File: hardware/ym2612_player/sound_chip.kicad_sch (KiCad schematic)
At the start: 30 parts, among them U3 74HCT541, U4 74HCT541, U5 YM2612 (socket only, chip fit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, X1 7.670454 MHz, 5V (not fitted)

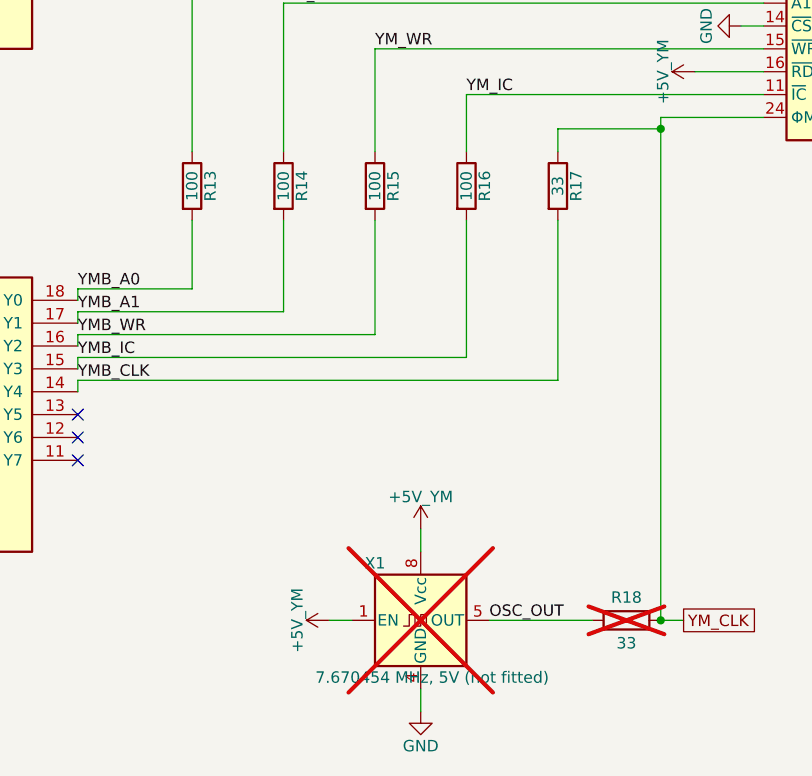
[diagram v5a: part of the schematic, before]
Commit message: Schematic: R13-R18 pin 1 back on the same net as on the board
The wired redraw drew R13-R17 upright and R18 turned, and swapped which net went to pin 1.
A resistor doesn't care, but KiCad's board-vs-schematic check flags it. Turn the symbols
instead, so every pin matches the board's pads again (checked pad by pad: 0 differences).

Co-Authored-By: Claude Opus 5.5 <noreply@anthropic.com>
Claude-Session: https://claude.ai/code/session_01TDTDVidYRoyJdUGgsyVTSw
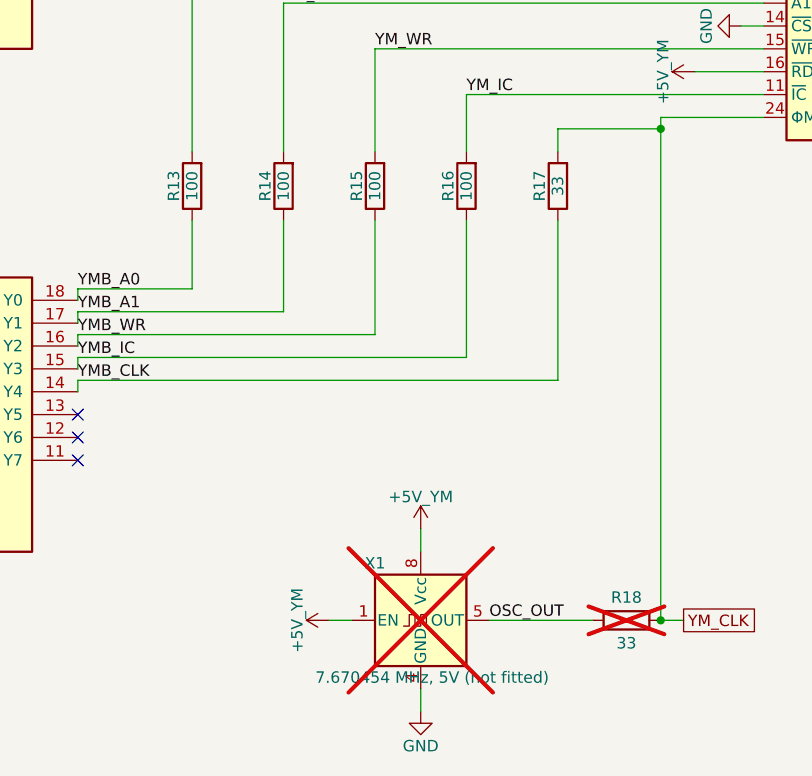
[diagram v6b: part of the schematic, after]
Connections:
- net OSC_OUT: now also R18.1; no longer R18.2
- net YMB_A0: now also R13.1; no longer R13.2
- net YMB_A1: now also R14.1; no longer R14.2
- net YMB_CLK: now also R17.1; no longer R17.2
- net YMB_IC: now also R16.1; no longer R16.2
- net YMB_WR: now also R15.1; no longer R15.2
- net YM_A0: now also R13.2; no longer R13.1
- net YM_A1: now also R14.2; no longer R14.1
- net YM_CLK: now also R17.2, R18.2; no longer R17.1, R18.1
- net YM_IC: now also R16.2; no longer R16.1
- net YM_WR: now also R15.2; no longer R15.1
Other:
- moved on the sheet: R13, R14, R15, R16, R17, R18
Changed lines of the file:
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@@
     )
   )
-  (symbol (lib_id "Device:R") (at 114.3 127 0) (unit 1)
+  (symbol (lib_id "Device:R") (at 114.3 127 180) (unit 1)
     (in_bom yes) (on_board yes) (dnp no)
-    (property "Reference" "R13" (at 116.332 127 90)
+    (property "Reference" "R13" (at 112.268 127 90)
       (effects (font (size 1.27 1.27)))
     )
@@
     )
   )
-  (symbol (lib_id "Device:R") (at 124.46 127 0) (unit 1)
+  (symbol (lib_id "Device:R") (at 124.46 127 180) (unit 1)
     (in_bom yes) (on_board yes) (dnp no)
-    (property "Reference" "R14" (at 126.492 127 90)
+    (property "Reference" "R14" (at 122.428 127 90)
       (effects (font (size 1.27 1.27)))
     )
@@
     )
   )
-  (symbol (lib_id "Device:R") (at 134.62 127 0) (unit 1)
+  (symbol (lib_id "Device:R") (at 134.62 127 180) (unit 1)
     (in_bom yes) (on_board yes) (dnp no)
-    (property "Reference" "R15" (at 136.652 127 90)
+    (property "Reference" "R15" (at 132.588 127 90)
       (effects (font (size 1.27 1.27)))
     )
@@
     )
   )
-  (symbol (lib_id "Device:R") (at 144.78 127 0) (unit 1)
+  (symbol (lib_id "Device:R") (at 144.78 127 180) (unit 1)
     (in_bom yes) (on_board yes) (dnp no)
-    (property "Reference" "R16" (at 146.812 127 90)
+    (property "Reference" "R16" (at 142.748 127 90)
       (effects (font (size 1.27 1.27)))
     )
@@
     )
   )
-  (symbol (lib_id "Device:R") (at 154.94 127 0) (unit 1)
+  (symbol (lib_id "Device:R") (at 154.94 127 180) (unit 1)
     (in_bom yes) (on_board yes) (dnp no)
-    (property "Reference" "R17" (at 156.972 127 90)
+    (property "Reference" "R17" (at 152.908 127 90)
       (effects (font (size 1.27 1.27)))
     )
@@
     )
   )
-  (symbol (lib_id "Device:R") (at 162.56 175.26 270) (unit 1)
+  (symbol (lib_id "Device:R") (at 162.56 175.26 90) (unit 1)
     (in_bom yes) (on_board yes) (dnp yes)
     (property "Reference" "R18" (at 162.56 172.72 90)
